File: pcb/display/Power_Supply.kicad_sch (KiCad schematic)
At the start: 60 parts, among them U10 TPS259474x, U11 LV3842, U6 AP2210, U9 SIC438BED-T1-GE3

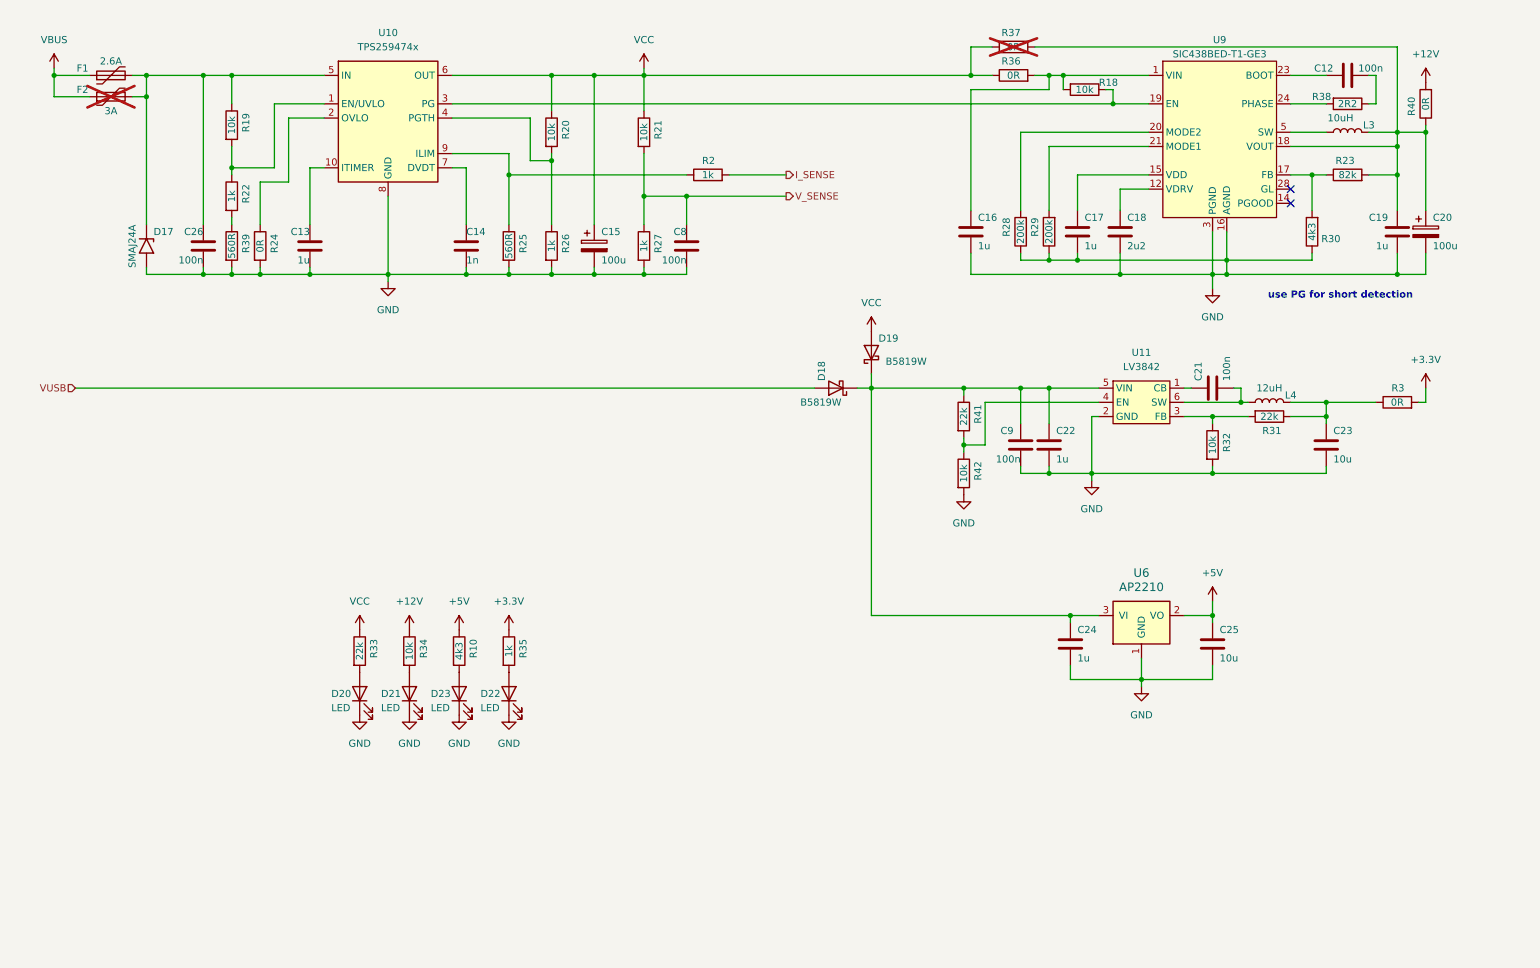
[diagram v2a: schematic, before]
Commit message: Display HW Revision 01
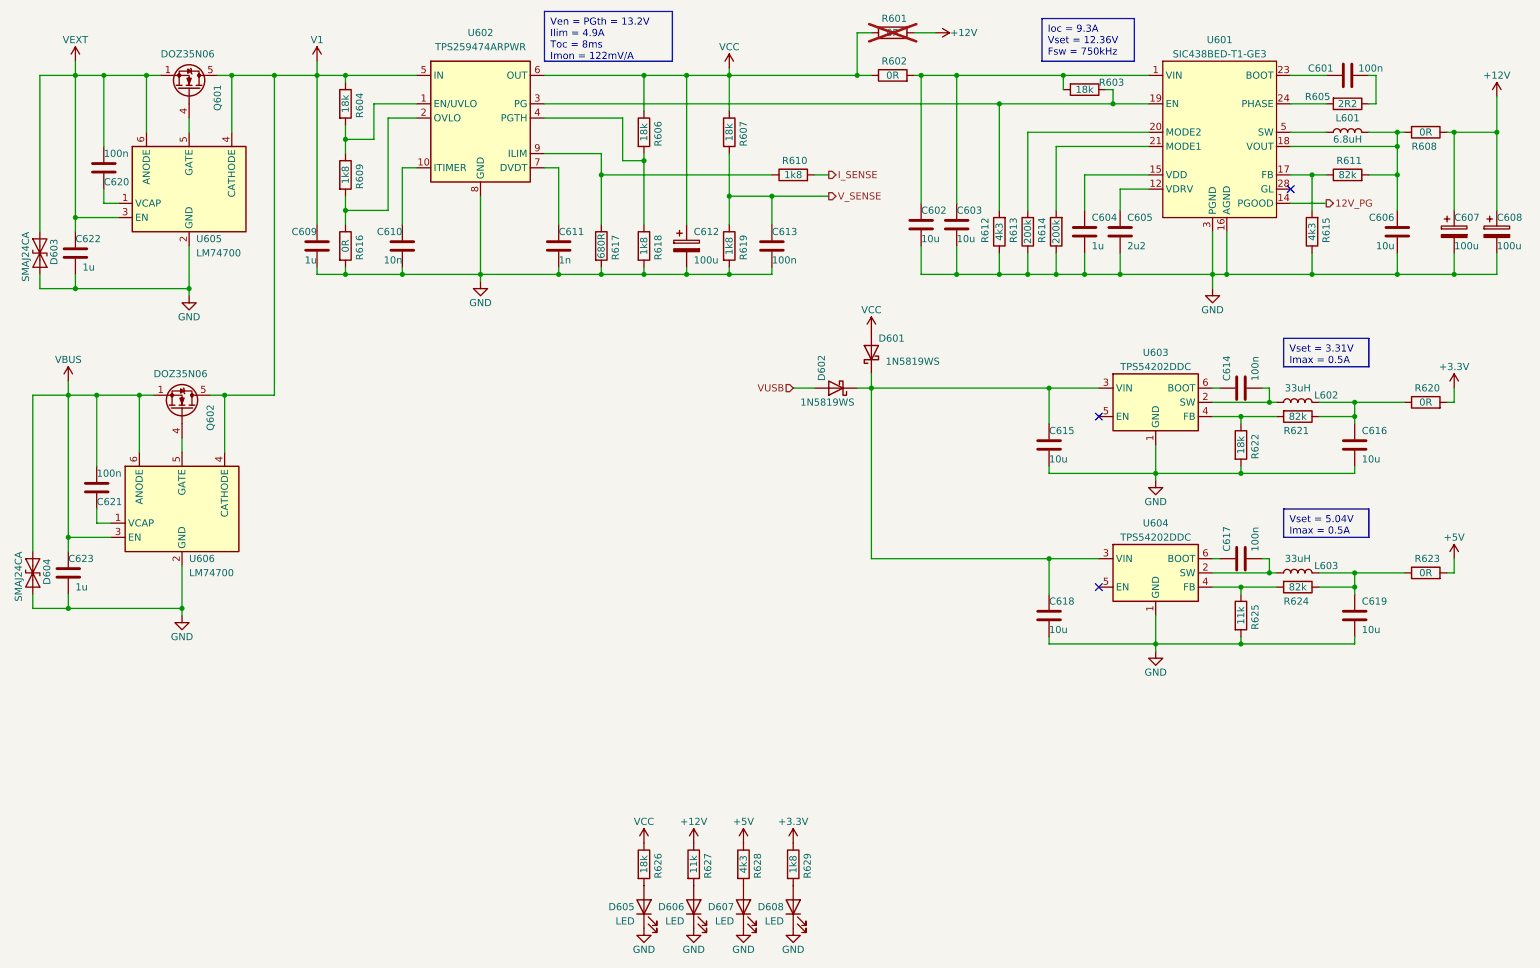
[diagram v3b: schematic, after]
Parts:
- removed C22, C24: 1u, Capacitor_SMD:C_0805_2012Metric, symbol Device:C
- removed C25: 10u, Capacitor_SMD:C_0805_2012Metric, symbol Device:C
- removed C9: 100n, Capacitor_SMD:C_0603_1608Metric, symbol Device:C
- removed D17: SMAJ24A, Diode_SMD:D_SMA, symbol Diode:SMAJ24A
- removed F1: 2.6A, Fuse:Fuse_2920_7451Metric, symbol Device:Polyfuse
- removed F2: 3A, Fuse:Fuse_Bourns_MF-RG400, symbol Device:Polyfuse
- removed R24: 0R, Resistor_SMD:R_0603_1608Metric, symbol Device:R
- removed R41: 22k, Resistor_SMD:R_0603_1608Metric, symbol Device:R
- removed R42: 10k, Resistor_SMD:R_0603_1608Metric, symbol Device:R
- removed U11: LV3842, Package_TO_SOT_SMD:SOT-23-6, symbol Ravenspark:LV3842
- removed U6: AP2210, Package_TO_SOT_SMD:SOT-23-3, symbol Ravenspark:AP2210
- added C602, C615, C618: 10u, Capacitor_SMD:C_1206_3216Metric, symbol Device:C
- added C608: 100u, Capacitor_SMD:CP_Elec_8x10, symbol Device:C_Polarized
- added C617, C620, C621: 100n, Capacitor_SMD:C_0402_1005Metric, symbol Device:C
- added C619: 10u, Capacitor_SMD:C_0603_1608Metric, symbol Device:C
- added C622, C623: 1u, Capacitor_SMD:C_0603_1608Metric, symbol Device:C
- added D603, D604: SMAJ24CA, Diode_SMD:D_SMA, symbol Diode:SMAJ24CA
- added L603: 33uH, Inductor_SMD:L_Changjiang_FNR4030S, symbol Device:L
- added Q601, Q602: DOZ35N06, Package_SON:VSON-8_3.3x3.3mm_P0.65mm_NexFET, symbol Ravenspark:60N03D
- added R612: 4k3, Resistor_SMD:R_0402_1005Metric, symbol Device:R
- added R623: 0R, Resistor_SMD:R_0603_1608Metric, symbol Device:R
- added R624: 82k, Resistor_SMD:R_0402_1005Metric, symbol Device:R
- added R625: 11k, Resistor_SMD:R_0402_1005Metric, symbol Device:R
- added U603, U604: TPS54202DDC, Package_TO_SOT_SMD:SOT-23-6, symbol Regulator_Switching:TPS54202DDC
- added U605, U606: LM74700, Package_TO_SOT_SMD:SOT-23-6, symbol Power_Management:LM74700
- C601: renamed from C12; footprint Capacitor_SMD:C_0603_1608Metric -> Capacitor_SMD:C_0402_1005Metric; JLC PN (none) -> C307331
- C603: renamed from C16; value 1u -> 10u; footprint Capacitor_SMD:C_0805_2012Metric -> Capacitor_SMD:C_1206_3216Metric; JLC PN (none) -> C13585
- C604: renamed from C17; JLC PN (none) -> C15849
- C605: renamed from C18; JLC PN (none) -> C23630
- C606: renamed from C19; value 1u -> 10u; footprint Capacitor_SMD:C_0805_2012Metric -> Capacitor_SMD:C_1206_3216Metric; JLC PN (none) -> C13585
- C607: renamed from C20; JLC PN (none) -> C5373402
- C609: renamed from C26; value 100n -> 1u; JLC PN (none) -> C15849
- C610: renamed from C13; value 1u -> 10n; footprint Capacitor_SMD:C_0603_1608Metric -> Capacitor_SMD:C_0402_1005Metric
- C611: renamed from C14; footprint Capacitor_SMD:C_0603_1608Metric -> Capacitor_SMD:C_0402_1005Metric
- C612: renamed from C15; JLC PN (none) -> C5373402
- C613: renamed from C8; footprint Capacitor_SMD:C_0603_1608Metric -> Capacitor_SMD:C_0402_1005Metric; JLC PN (none) -> C307331
- C614: renamed from C21; footprint Capacitor_SMD:C_0603_1608Metric -> Capacitor_SMD:C_0402_1005Metric; JLC PN (none) -> C307331
- C616: renamed from C23; footprint Capacitor_SMD:C_0805_2012Metric -> Capacitor_SMD:C_0603_1608Metric; JLC PN (none) -> C19702
- D601: renamed from D19; value B5819W -> 1N5819WS; footprint Diode_SMD:D_SOD-123 -> Diode_SMD:D_SOD-323; JLC PN (none) -> C191023
- D602: renamed from D18; value B5819W -> 1N5819WS; footprint Diode_SMD:D_SOD-123 -> Diode_SMD:D_SOD-323; JLC PN (none) -> C191023
- D605: renamed from D20; JLC PN (none) -> C2286
- D606: renamed from D21; JLC PN (none) -> C2286
- D607: renamed from D23; JLC PN (none) -> C2286
- D608: renamed from D22; JLC PN (none) -> C2286
- L601: renamed from L3; value 10uH -> 6.8uH; footprint Inductor_SMD:L_Bourns_SRR1260 -> Inductor_SMD:L_Bourns_SRP1050WA; JLC PN (none) -> C32712978
- L602: renamed from L4; value 12uH -> 33uH; footprint Inductor_SMD:L_Changjiang_FNR6045S -> Inductor_SMD:L_Changjiang_FNR4030S; JLC PN (none) -> C5291825
- R601: renamed from R37; footprint Resistor_SMD:R_0805_2012Metric -> Resistor_SMD:R_1206_3216Metric
- R602: renamed from R36; footprint Resistor_SMD:R_0805_2012Metric -> Resistor_SMD:R_1206_3216Metric
- R603: renamed from R18; value 10k -> 18k; footprint Resistor_SMD:R_0603_1608Metric -> Resistor_SMD:R_0402_1005Metric
- R604: renamed from R19; value 10k -> 18k; footprint Resistor_SMD:R_0603_1608Metric -> Resistor_SMD:R_0402_1005Metric
- R605: renamed from R38; footprint Resistor_SMD:R_0603_1608Metric -> Resistor_SMD:R_0402_1005Metric
- R606: renamed from R20; value 10k -> 18k; footprint Resistor_SMD:R_0603_1608Metric -> Resistor_SMD:R_0402_1005Metric
- R607: renamed from R21; value 10k -> 18k; footprint Resistor_SMD:R_0603_1608Metric -> Resistor_SMD:R_0402_1005Metric
- R608: renamed from R40; footprint Resistor_SMD:R_0805_2012Metric -> Resistor_SMD:R_1206_3216Metric
- R609: renamed from R22; value 1k -> 1k8; footprint Resistor_SMD:R_0603_1608Metric -> Resistor_SMD:R_0402_1005Metric
- R610: renamed from R2; value 1k -> 1k8; footprint Resistor_SMD:R_0603_1608Metric -> Resistor_SMD:R_0402_1005Metric
- R611: renamed from R23; footprint Resistor_SMD:R_0603_1608Metric -> Resistor_SMD:R_0402_1005Metric
- R613: renamed from R28; footprint Resistor_SMD:R_0603_1608Metric -> Resistor_SMD:R_0402_1005Metric
- R614: renamed from R29; footprint Resistor_SMD:R_0603_1608Metric -> Resistor_SMD:R_0402_1005Metric
- R615: renamed from R30; footprint Resistor_SMD:R_0603_1608Metric -> Resistor_SMD:R_0402_1005Metric
- R616: renamed from R39; value 560R -> 0R; footprint Resistor_SMD:R_0603_1608Metric -> Resistor_SMD:R_0402_1005Metric
- R617: renamed from R25; value 560R -> 680R; footprint Resistor_SMD:R_0603_1608Metric -> Resistor_SMD:R_0402_1005Metric
- R618: renamed from R26; value 1k -> 1k8; footprint Resistor_SMD:R_0603_1608Metric -> Resistor_SMD:R_0402_1005Metric
- R619: renamed from R27; value 1k -> 1k8; footprint Resistor_SMD:R_0603_1608Metric -> Resistor_SMD:R_0402_1005Metric
- R620: renamed from R3; footprint Resistor_SMD:R_0805_2012Metric -> Resistor_SMD:R_0603_1608Metric
- R621: renamed from R31; value 22k -> 82k; footprint Resistor_SMD:R_0603_1608Metric -> Resistor_SMD:R_0402_1005Metric
- R622: renamed from R32; value 10k -> 18k; footprint Resistor_SMD:R_0603_1608Metric -> Resistor_SMD:R_0402_1005Metric
- R626: renamed from R33; value 22k -> 18k; footprint Resistor_SMD:R_0603_1608Metric -> Resistor_SMD:R_0402_1005Metric
- R627: renamed from R34; value 10k -> 11k; footprint Resistor_SMD:R_0603_1608Metric -> Resistor_SMD:R_0402_1005Metric
- R628: renamed from R10; footprint Resistor_SMD:R_0603_1608Metric -> Resistor_SMD:R_0402_1005Metric
- R629: renamed from R35; value 1k -> 1k8; footprint Resistor_SMD:R_0603_1608Metric -> Resistor_SMD:R_0402_1005Metric
- U601: renamed from U9; JLC PN (none) -> C511430
- U602: renamed from U10; value TPS259474x -> TPS259474ARPWR; JLC PN (none) -> C3662807
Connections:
- net +12V: now also C607.1, R601.2, R608.1, C608.1; no longer R608.2
- net +5V: now also R623.2
- net AGND: now also C602.2, C608.2, C615.2, C618.2, C619.2, C622.2, C623.2, D603.2 (A2), D604.2 (A2), R612.1, R625.2, U603.1 (GND), U604.1 (GND), U605.2 (GND), U606.2 (GND)
- net VBUS: now also C621.1, C623.1, D604.1 (A1), Q602.1 (S), Q602.2 (S), Q602.3 (S), U606.3 (EN), U606.6 (ANODE)
- net VIN: now also C602.1
- net at U602.2 (OVLO): now also R609.2, R616.1
- net at D601.1 (K), D602.1 (K): now also C615.1, C618.1, U603.3 (VIN), U604.3 (VIN)
- net at C614.2, L602.1: now also U603.2 (SW)
- net at R603.1, U601.19 (EN), U602.3 (PG): now also R612.2
- net at C606.1, L601.2, R611.2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: now also R608.2; no longer C607.1, R601.2, R608.1
- net V1: now reaches C609.2, R604.1, U602.5 (IN)
- net V1: now also Q601.5 (D), Q602.5 (D), U605.4 (CATHODE), U606.4 (CATHODE)
- net 12V_PG: now reaches U601.14 (PGOOD)
- net at R621.2, R622.1: now also U603.4 (FB)
- net at C614.1: now also U603.6 (BOOT)
- new net: C619.1, L603.2, R623.1, R624.1
- new net: C621.2, U606.1 (VCAP)
- new net: Q602.4 (G), U606.5 (GATE)
- new net: C617.2, L603.1, U604.2 (SW)
- new net: C620.2, U605.1 (VCAP)
- new net: Q601.4 (G), U605.5 (GATE)
- new net: C617.1, U604.6 (BOOT)
- new net: R624.2, R625.1, U604.4 (FB)
- new net VEXT: C620.1, C622.1, D603.1 (A1), Q601.1 (S), Q601.2 (S), Q601.3 (S), U605.3 (EN), U605.6 (ANODE)
- no-connect marks 2 -> 3
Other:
- note removed: "use PG for short detection"
- moved on the sheet: C603, C604, C607, C609, C610, C611, C612, C613, C614, C616, D605, D606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

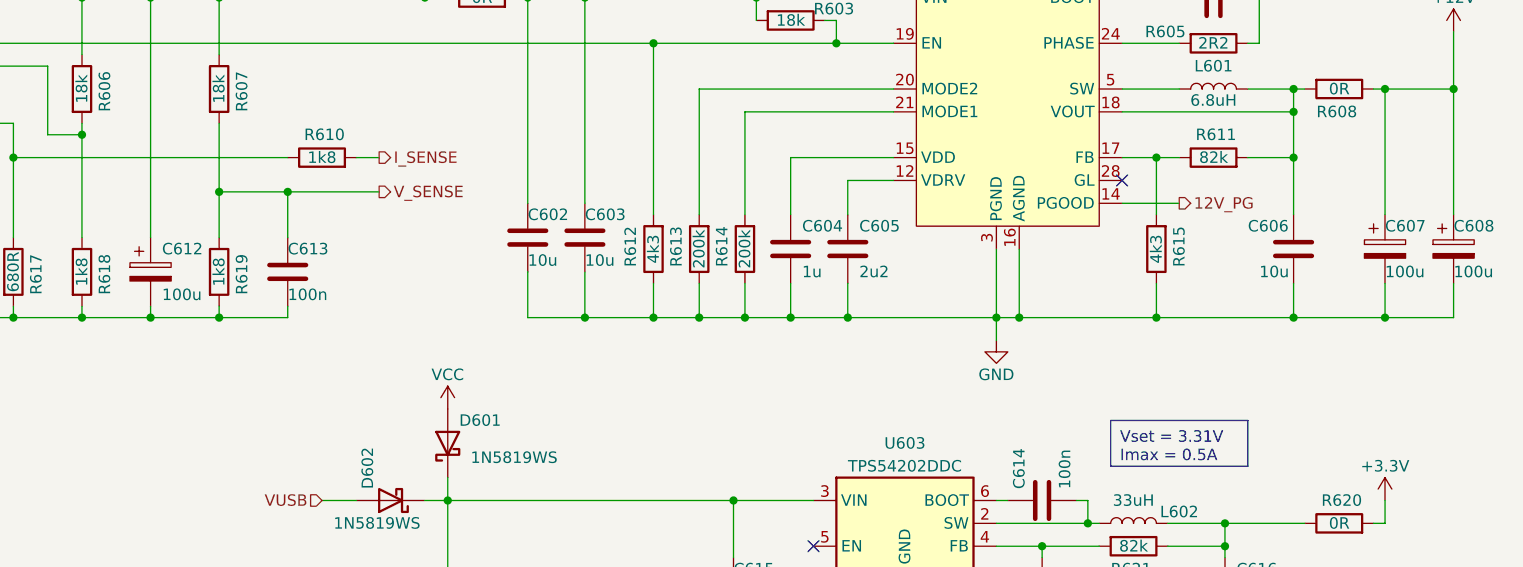
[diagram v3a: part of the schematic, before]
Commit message: Update some wrong values after import in JLC for production
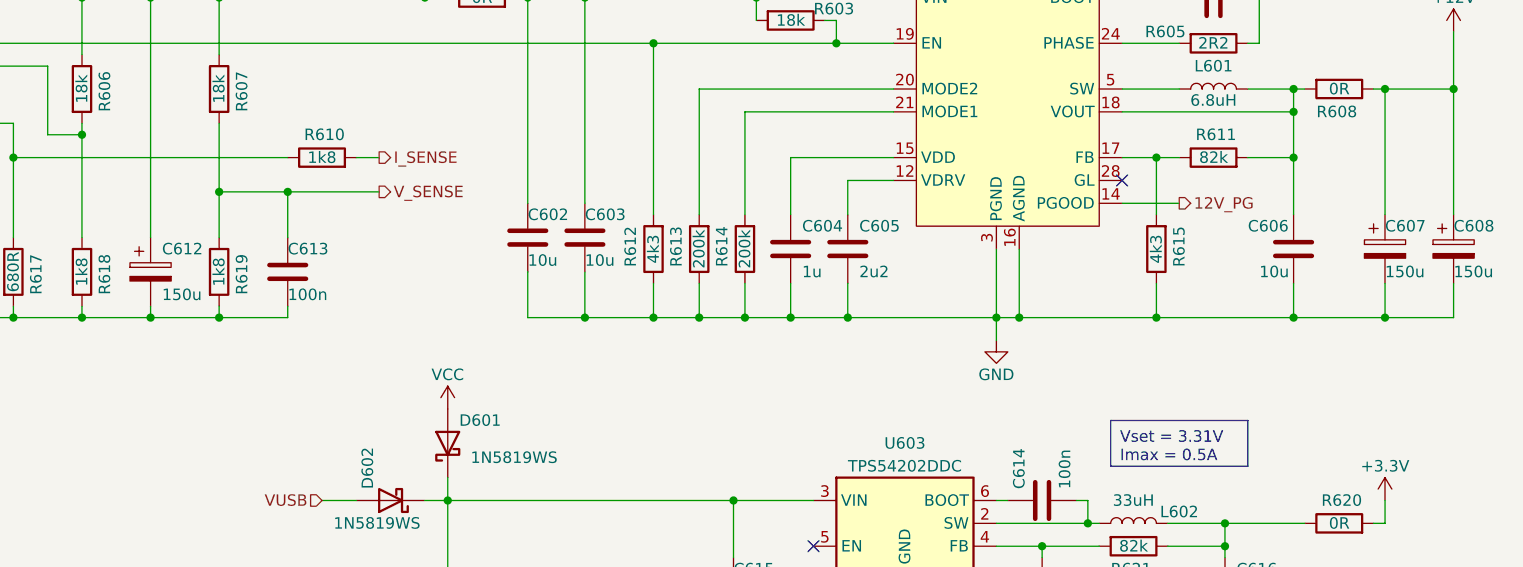
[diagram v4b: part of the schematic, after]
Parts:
- C607, C608, C612: value 100u -> 150u
- C610: JLC PN (none) -> C15195
- C611: JLC PN (none) -> C1523
- L602, L603: JLC PN C5291825 -> C15269
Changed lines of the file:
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@@
 	(title_block
 		(title "Power Supply")
-		(date "2025-04-08")
+		(date "2025-04-11")
 		(rev "01")
 		(company "Ravenspark")
@@
 			)
 		)
-		(property "JLC PN" "C5291825"
+		(property "JLC PN" "C15269"
 			(at 243.84 83.82 0)
 			(effects
@@
 			)
 		)
-		(property "JLC PN" "C5291825"
+		(property "JLC PN" "C15269"
 			(at 243.84 114.3 0)
 			(effects
@@
 			)
 		)
+		(property "JLC PN" "C1523"
+			(at 111.76 55.88 0)
+			(effects
+				(font
+					(size 1.27 1.27)
+				)
+				(hide yes)
+			)
+		)
 		(pin "2"
 		)
@@
 			)
 		)
-		(property "Value" "100u"
+		(property "Value" "150u"
 			(at 271.78 55.88 0)
 			(effects
@@
 			)
 		)
-		(property "Value" "100u"
+		(property "Value" "150u"
 			(at 279.4 55.88 0)
 			(effects
@@
 			)
 		)
-		(property "Value" "100u"
+		(property "Value" "150u"
 			(at 135.89 58.42 0)
 			(effects
@@
 			(at 83.82 55.88 0)
 			(effects
+				(font
+					(size 1.27 1.27)
+				)
+				(hide yes)
+			)
+		)
+		(property "JLC PN" "C15195"
+			(at 83.82 55.88 0)
+			(effects
